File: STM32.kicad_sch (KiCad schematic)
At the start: 41 parts, among them IC201 ESDALC6V1W5, IC202 ESDALC6V1W5, IC203 ESDALC6V1W5, J206 Conn_01x04_Pin, J207 Conn_01x07_Pin, Q201 DMG1012T-13, Q202 DMG1012T-13, Q203 DMG1012T-13, Q204 DMG1012T-13, U201 TLV9304IDR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

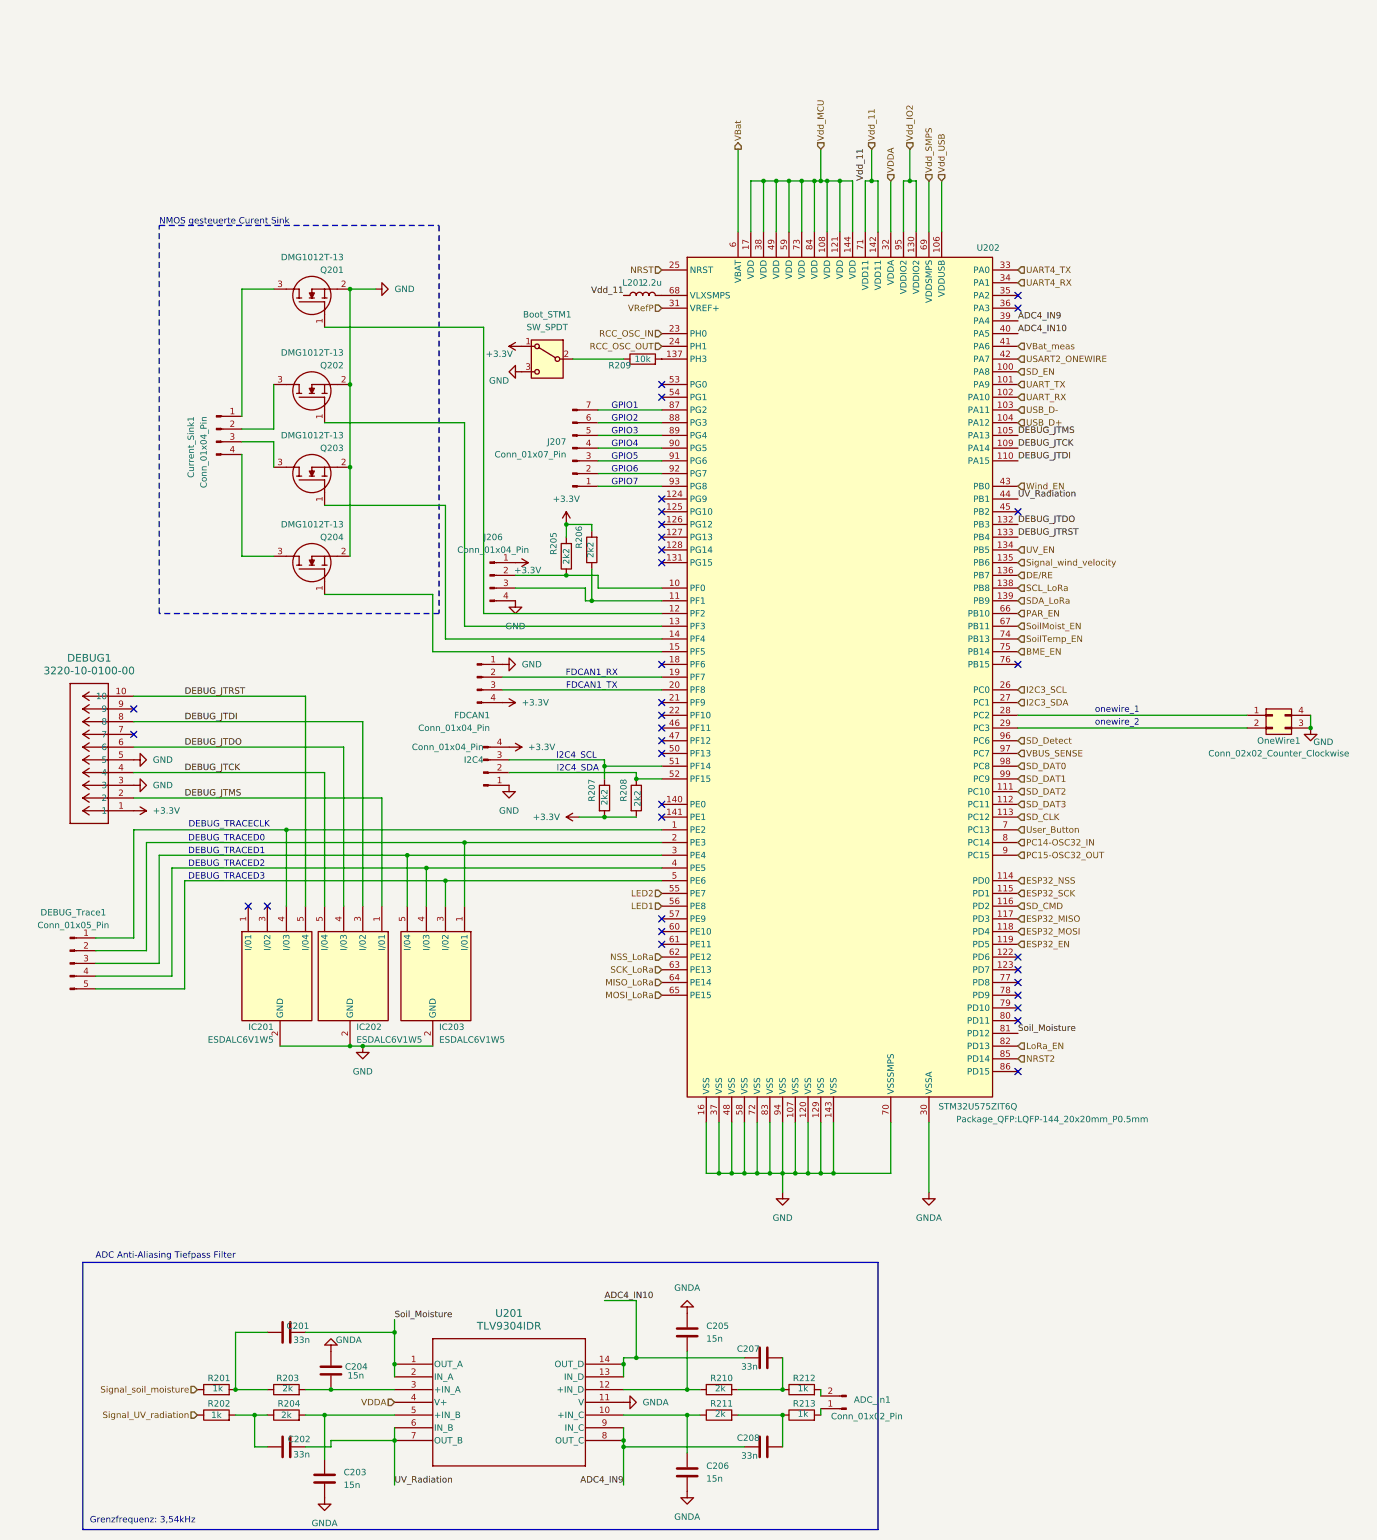
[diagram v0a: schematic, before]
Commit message: Add FC0V104ZFTBR24 component library files
Added symbol, footprint, 3D model, and documentation files for the Supercap (FC0V104ZFTBR24) component across multiple EDA tool formats. Also updated schematic files and project backups, and removed obsolete autosave and backup files.
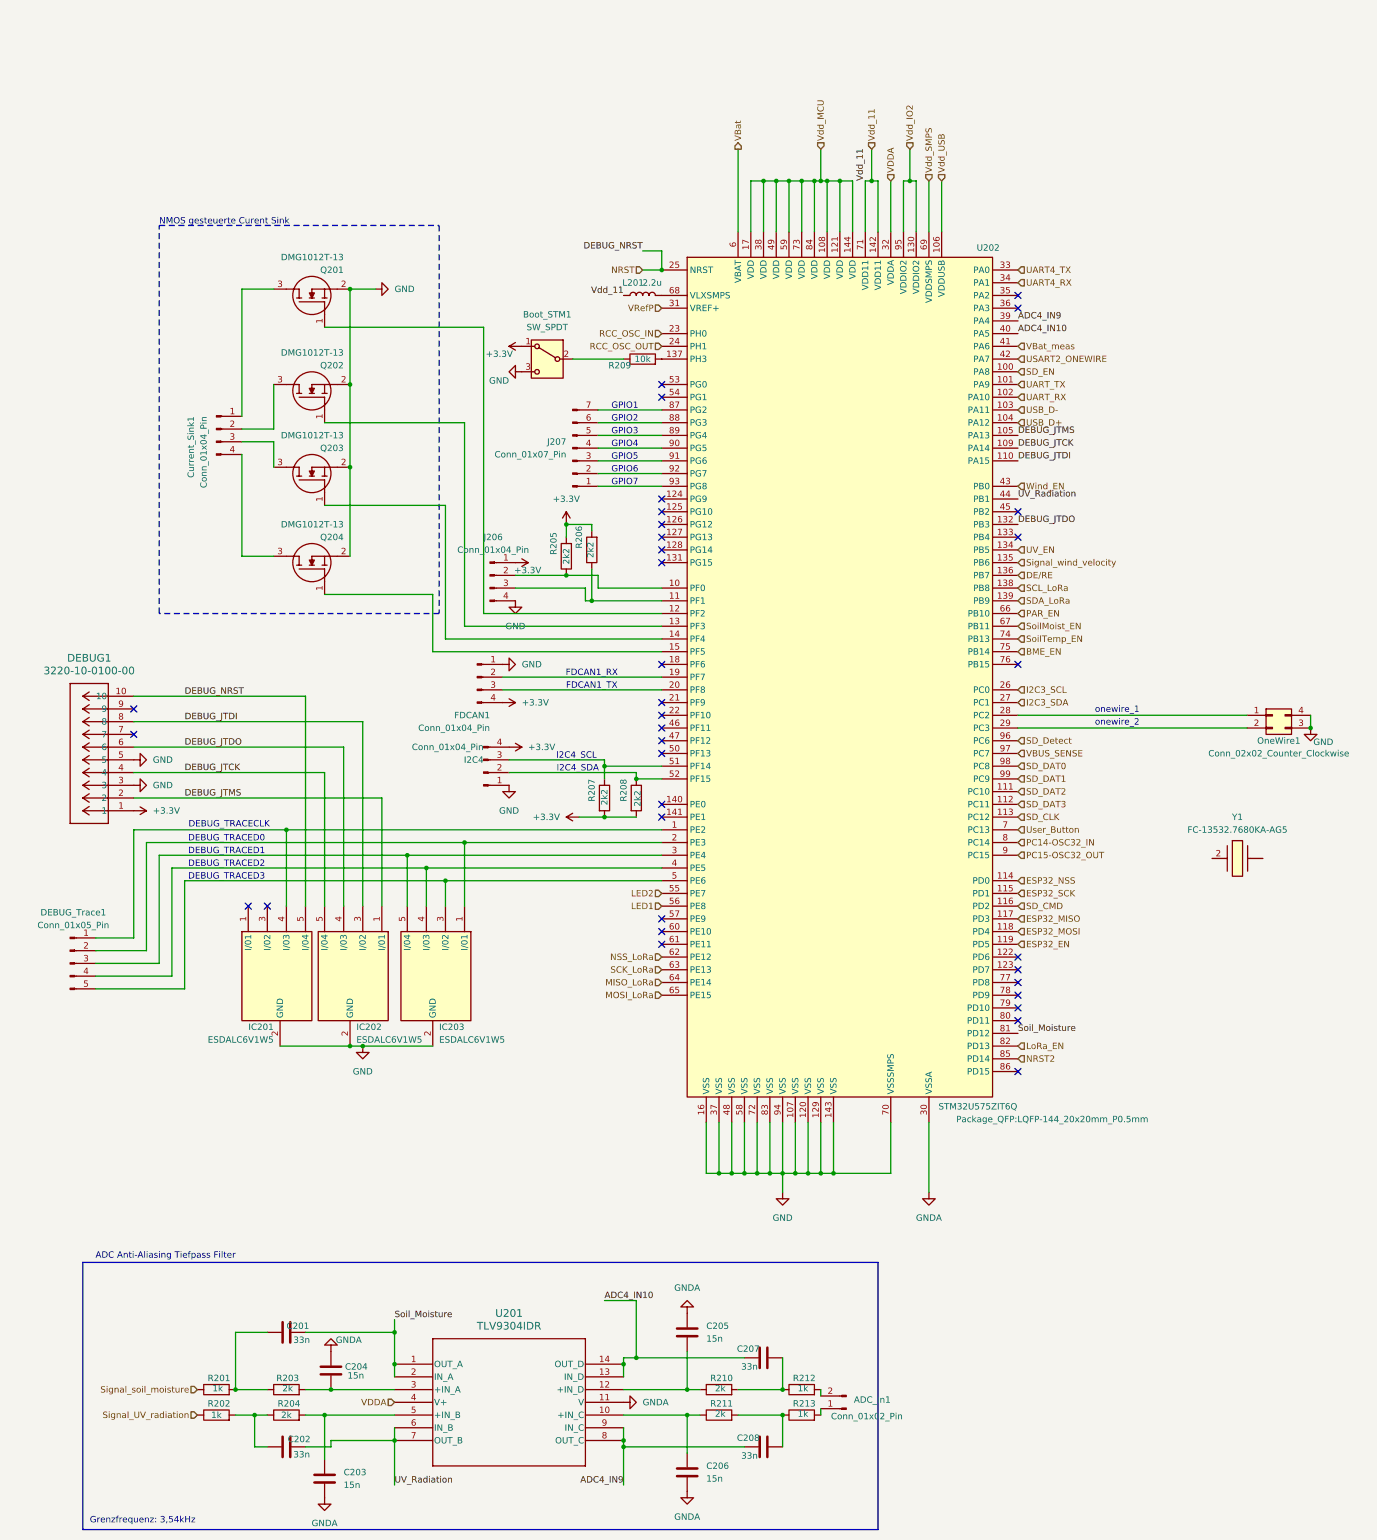
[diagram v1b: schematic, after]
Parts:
- added Y1: FC-13532.7680KA-AG5, FC135327680KAAG5, symbol SamacSys_Parts:FC-13532.7680KA-AG5
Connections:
- net NRST: now also DEBUG1.10, IC201.5 (I/04)
- removed net DEBUG_JTRST: DEBUG1.10, IC201.5 (I/04), U202.133 (PB4)
- no-connect marks 34 -> 35
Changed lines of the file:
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@@
 	)
 	(junction
+		(at 144.78 83.82)
+		(diameter 0)
+		(color 0 0 0 0)
+	)
+	(junction
 		(at 91.44 295.91)
 		(diameter 0)
@@
 	)
 	(no_connect
+		(at 215.9 137.16)
+	)
+	(no_connect
 		(at 144.78 129.54)
 	)
@@
 	(wire
 		(pts
+			(xy 140.97 80.01) (xy 144.78 80.01)
+		)
+		(stroke
+			(width 0)
+			(type default)
+		)
+	)
+	(wire
+		(pts
 			(xy 78.74 307.34) (xy 91.44 307.34)
 		)
@@
 	(wire
 		(pts
+			(xy 140.97 83.82) (xy 144.78 83.82)
+		)
+		(stroke
+			(width 0)
+			(type default)
+		)
+	)
+	(wire
+		(pts
 			(xy 144.78 154.94) (xy 105.41 154.94)
 		)
@@
 	(wire
 		(pts
+			(xy 144.78 80.01) (xy 144.78 83.82)
+		)
+		(stroke
+			(width 0)
+			(type default)
+		)
+	)
+	(wire
+		(pts
 			(xy 139.7 185.42) (xy 144.78 185.42)
 		)
@@
 		)
 	)
-	(label "DEBUG_JTRST"
+	(label "DEBUG_NRST"
 		(at 49.53 168.91 0)
 		(effects
@@
 		)
 	)
+	(label "DEBUG_NRST"
+		(at 140.97 80.01 180)
+		(effects
+			(font
+				(size 1.27 1.27)
+			)
+			(justify right bottom)
+		)
+	)
 	(label "ADC4_IN10"
 		(at 133.35 289.56 0)
@@
 		)
 	)
-	(label "DEBUG_JTRST"
-		(at 215.9 137.16 0)
-		(effects
-			(font
-				(size 1.27 1.27)
-			)
-			(justify left bottom)
-		)
-	)
 	(label "ADC4_IN9"
 		(at 137.16 326.39 180)
@@
 	(hierarchical_label "NRST"
 		(shape input)
-		(at 144.78 83.82 180)
+		(at 140.97 83.82 180)
 		(effects
 			(font
@@
 					(unit 1)
 				)
+			)
+		)
+	)
+	(symbol
+		(lib_id "SamacSys_Parts:FC-13532.7680KA-AG5")
+		(at 254.635 201.295 0)
+		(unit 1)
+		(exclude_from_sim no)
+		(in_bom yes)
+		(on_board yes)
+		(dnp no)
+		(fields_autoplaced yes)
+		(property "Reference" "Y1"
+			(at 259.715 193.04 0)
+			(effects
+				(font
+					(size 1.27 1.27)
+				)
+			)
+		)
+		(property "Value" "FC-13532.7680KA-AG5"
+			(at 259.715 195.58 0)
+			(effects
+				(font
+					(size 1.27 1.27)
+				)
+			)
+		)
+		(property "Footprint" "FC135327680KAAG5"
+			(at 263.525 297.485 0)
+			(effects
+				(font
+					(size 1.27 1.27)
+				)
+				(justify left top)
+				(hide yes)
+			)
+		)
+		(property "Datasheet" "https://support.epson.biz/td/api/doc_check.php?dl=brief_FC-135&lang=en"
+			(at 263.525 397.485 0)
+			(effects
+				(font
+					(size 1.27 1.27)
+				)
+				(justify left top)
+				(hide yes)
+			)
+		)
+		(property "Description" "32.768kHz +/-20ppm Crystal 7pF 70 kOhms 2-SMD, No Lead"
+			(at 254.635 201.295 0)
+			(effects
+				(font
+					(size 1.27 1.27)
+				)
+				(hide yes)
+			)
+		)
+		(property "Height" "0.9"
+			(at 263.525 597.485 0)
+			(effects
+				(font
+					(size 1.27 1.27)
+				)
+				(justify left top)
+				(hide yes)
+			)
+		)
+		(property "Mouser Part Number" ""
+			(at 263.525 697.485 0)
+			(effects
+				(font
+					(size 1.27 1.27)
+				)
+				(justify left top)
+				(hide yes)
+			)
+		)
+		(property "Mouser Price/Stock" ""
+			(at 263.525 797.485 0)
+			(effects
+				(font
+					(size 1.27 1.27)
+				)
+				(justify left top)
+				(hide yes)
+			)
+		)
+		(property "Manufacturer_Name" "Seiko Epson Corporation"
+			(at 263.525 897.485 0)
+			(effects
+				(font
+					(size 1.27 1.27)
+				)
+				(justify left top)
+				(hide yes)
+			)
+		)
+		(property "Manufacturer_Part_Number" "FC-13532.7680KA-AG5"
+			(at 263.525 997.485 0)
+			(effects
+				(font
+					(size 1.27 1.27)
+				)
+				(justify left top)
+				(hide yes)
+			)
+		)
+		(pin ""
+		)
+		(pin "2"
+		)
+		(instances
+			(project ""
+				(path "/69abffa1-550c-4cd8-ae80-a1755923d6dc/68eeaf65-50b7-4f21-91a4-9a8eefc615e6"
+					(reference "Y1")
+					(unit 1)
+				)
